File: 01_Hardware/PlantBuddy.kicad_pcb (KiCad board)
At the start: 2 copper layers, 35 x 87.3 mm, 36 parts, among them J101 J-Link SWD, J102 NFC Antenna, J2 Conn_I2C_SDA, J3 Conn_I2C_SCL, Q101 AO3401A, U101 nRF52832-QFxx, U102 LTR-303ALS-01, U6 SHTC3, Y1 32MHz, Y2 32kHz

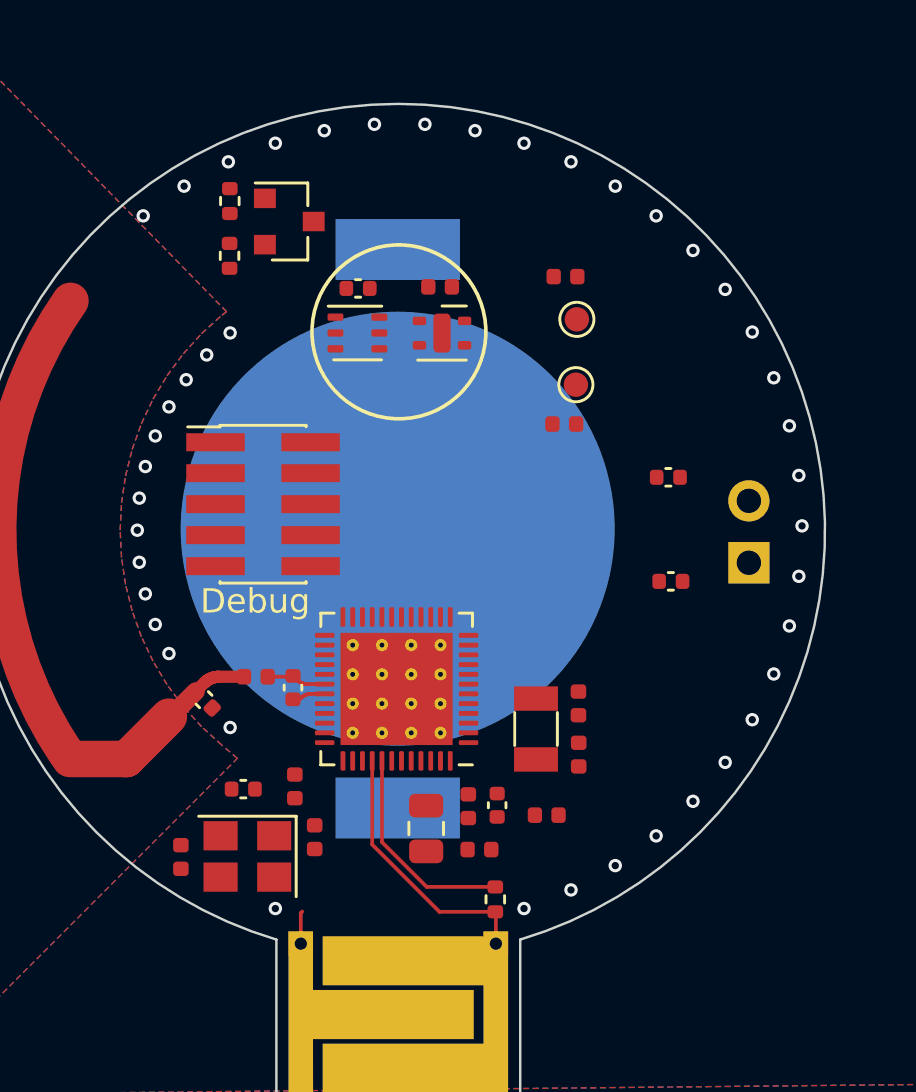
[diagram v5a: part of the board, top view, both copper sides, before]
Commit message: Switched to 0603 and re-did layout.
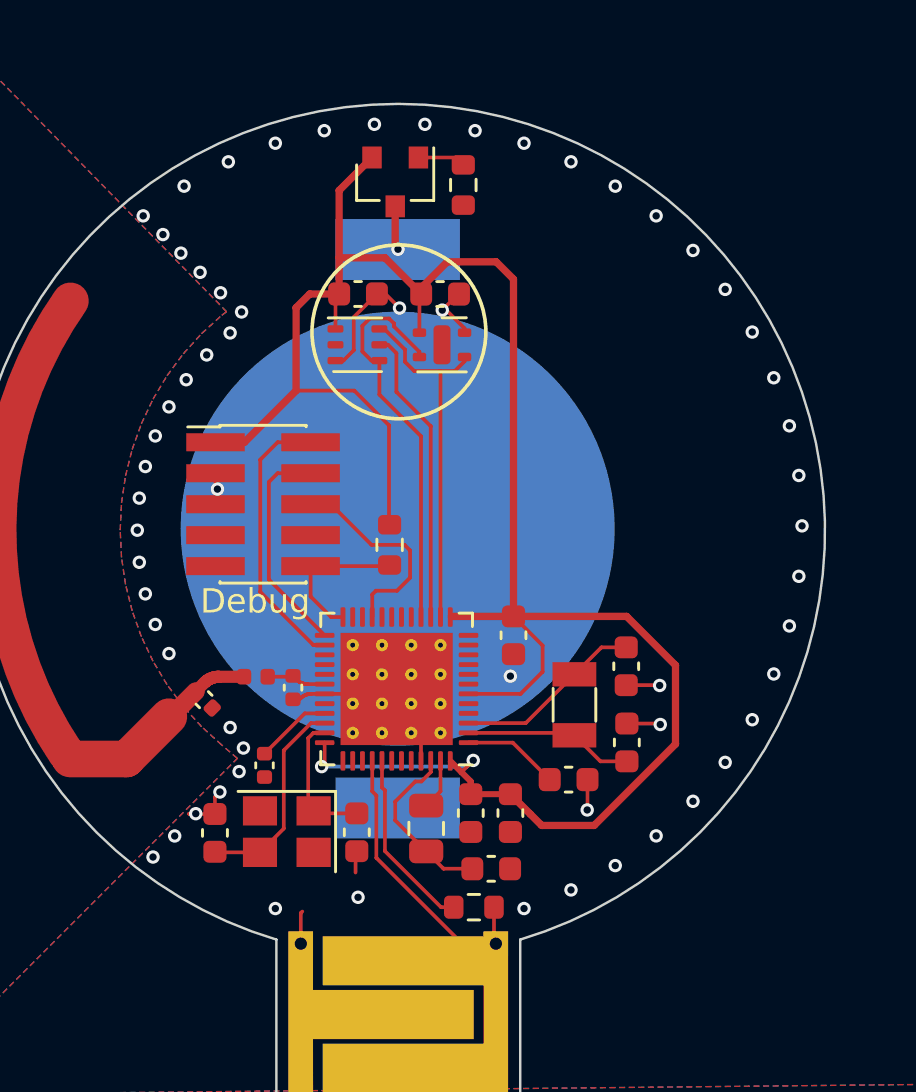
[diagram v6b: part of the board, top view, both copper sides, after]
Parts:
- removed C101, C102: N/P, Capacitor_SMD:C_0402_1005Metric
- removed J102: NFC Antenna, Connector_PinHeader_2.54mm:PinHeader_1x02_P2.54mm_Vertical
- removed J2: Conn_I2C_SDA, TestPoint:TestPoint_Pad_D1.0mm
- removed J3: Conn_I2C_SCL, TestPoint:TestPoint_Pad_D1.0mm
- removed R14, R15: 10k, Resistor_SMD:R_0402_1005Metric
- C10, C11, C12, C13, C14, C15, C16, C17, C3, C5, C6: footprint Capacitor_SMD:C_0402_1005Metric -> Capacitor_SMD:C_0603_1608Metric
- R1, R4: footprint Resistor_SMD:R_0402_1005Metric -> Resistor_SMD:R_0603_1608Metric
- R101: value 100k -> 3M3; footprint Resistor_SMD:R_0402_1005Metric -> Resistor_SMD:R_0603_1608Metric
- moved R1 13.5 mm to (65.4, 65.0)
- moved C10 10.9 mm to (70.4, 68.7)
- moved R4 9.60 mm to (68.4, 50.3)
- moved Q101 4.64 mm to (65.6, 50.1), turned to 270 degrees
- moved C13 2.48 mm to (75.1, 70.0)
- moved C14 2.04 mm to (75.1, 73.1)
- moved Y1 1.91 mm to (61.1, 76.8)
- moved Y2 1.86 mm to (72.9, 71.6)
- moved C6 1.74 mm to (64.0, 76.8)
- moved C5 1.71 mm to (72.7, 74.6)
- moved C11 1.71 mm to (58.2, 76.8)
- moved C9 1.31 mm to (60.2, 74.1), turned to 90 degrees
- moved R101 0.94 mm to (68.8, 79.9), turned to 0 degrees
- moved C16 0.92 mm to (69.5, 78.3)
- moved C15 0.63 mm to (70.3, 76.0)
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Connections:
- J101 pad 9: +BATT -> Net-(J101-Pad9)
- U101 pad 15: /SCL -> /LUX_INT
- U101 pad 16: Net-(U101-Pad16) -> /SCL
- U101 pad 18: /LUX_INT -> Net-(U101-Pad18)
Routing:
- net +BATT: track 0.00 -> 89.5 mm, vias 0 -> 2
- net GND: track 2.71 -> 24.5 mm, vias 43 -> 62
- net /SCL: track 0.00 -> 16.4 mm
- net /SDA: track 0.00 -> 14.9 mm
- net /LUX_INT: track 0.00 -> 12.2 mm
- net /SWDIO: track 0.00 -> 11.3 mm
- net /SWCLK: track 0.00 -> 9.10 mm
- net /SWO: track 0.00 -> 8.74 mm
- net /XC1: track 0.00 -> 8.58 mm
- net /XL2: track 0.00 -> 7.75 mm
- net Net-(C16-Pad2): track 0.00 -> 7.17 mm
- net /XL1: track 0.00 -> 6.98 mm
- net /~RST: track 0.00 -> 6.18 mm
- net /XC2: track 0.00 -> 5.60 mm
- net Net-(C5-Pad2): track 0.00 -> 3.96 mm
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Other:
- board text removed: "NFC"

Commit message: Done with latest HW revision. To be ordered with Aisler.
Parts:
- added LS101: Speaker_Crystal, Connector_PinHeader_2.54mm:PinHeader_1x02_P2.54mm_Vertical, F.Cu at (79.9, 65.4)
- moved C14 1.40 mm to (76.5, 73.1)
- moved Y2 1.40 mm to (74.3, 71.6)
- moved C13 1.40 mm to (76.5, 70.0)
- moved C5 1.40 mm to (74.1, 74.6)
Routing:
- net Net-(LS101-Pad2): track 0.00 -> 16.1 mm, vias 0 -> 2
- net Net-(LS101-Pad1): track 0.00 -> 15.7 mm, vias 0 -> 2
- net +BATT: track 89.5 -> 96.6 mm
- net /XL1: track 6.98 -> 8.37 mm
- net Net-(C5-Pad2): track 3.96 -> 5.35 mm
- net /XL2: track 7.75 -> 9.15 mm
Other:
- board text added: "FlivzNexxy"
- board text added: "Piezo"
- board text removed: "PlantBuddy"

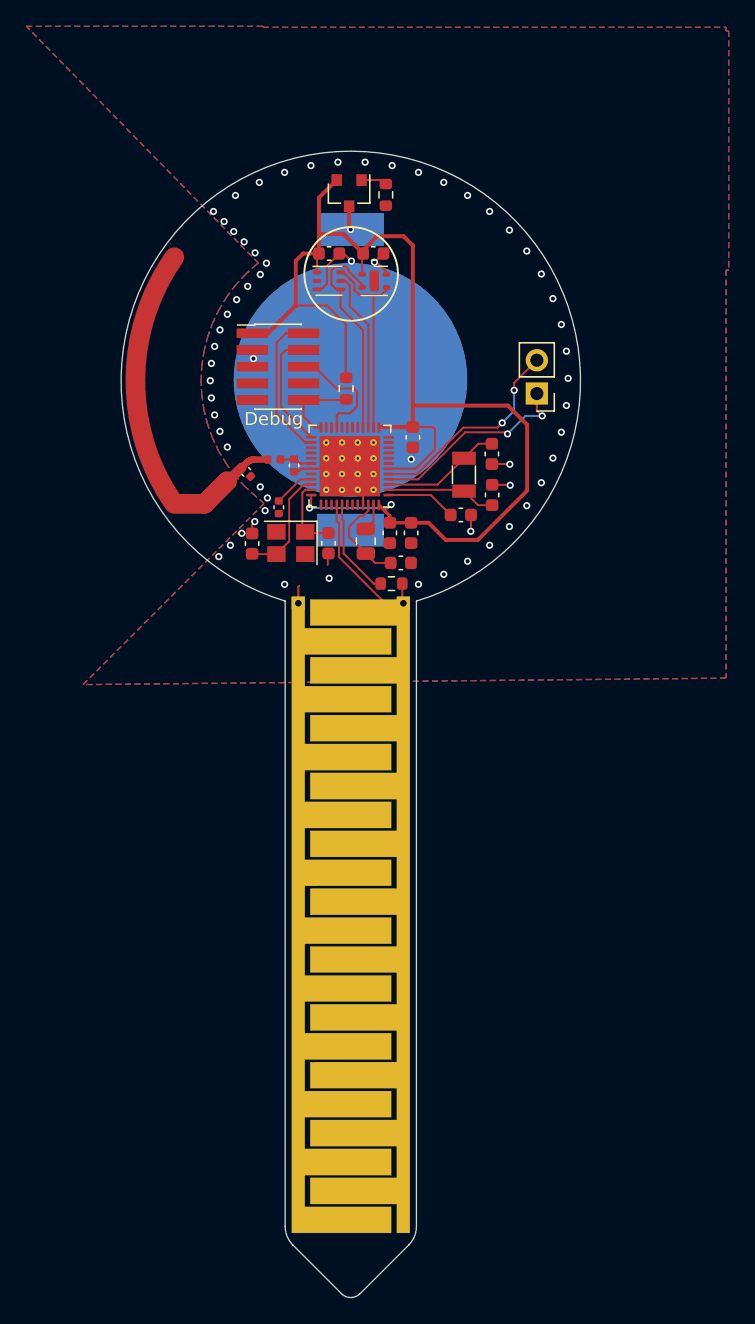
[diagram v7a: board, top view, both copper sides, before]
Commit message: Slight adjustments to Antenna ground plane & length.
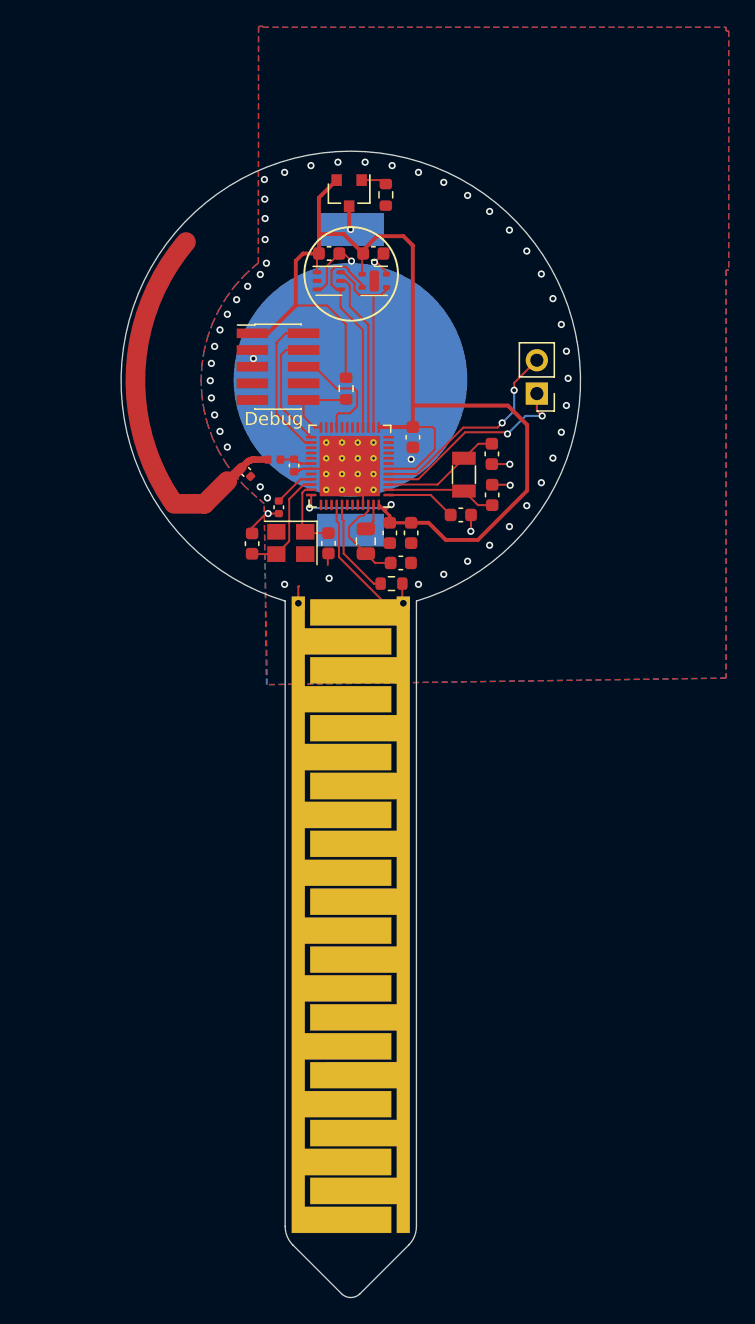
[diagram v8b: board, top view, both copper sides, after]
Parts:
- turned AE101 to 139.9 degrees
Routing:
- net GND: track 24.5 -> 25.4 mm, vias 62 -> 55
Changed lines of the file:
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@@
     (thickness 1.6)
     (drawings 21)
-    (tracks 328)
+    (tracks 321)
     (zones 0)
     (modules 30)
@@
     (uvia_drill 0.1)
   )
+  (module PlantBuddy:monopole (layer F.Cu)
+    (at 65.7098 64.4144 139.9)
+    (fp_text reference AE101 (at 0 0 319.9) (layer F.SilkS) hide
+      (effects (font (size 1.27 1.27) (thickness 0.15)))
+    )
+    (fp_text value Antenna (at 0 0 319.9) (layer F.SilkS) hide
+      (effects (font (size 1.27 1.27) (thickness 0.15)))
+    )
+    (fp_arc (start 0 0) (end 16.4 0) (angle -74) (layer F.Cu) (width 1.5))
+  )
   (module Connector_PinHeader_2.54mm:PinHeader_1x02_P2.54mm_Vertical (layer F.Cu)
     (at 79.89228 65.396371 180)
@@
     )
     (fp_text value Speaker_Crystal (at 0 4.87) (layer F.Fab)
-      (effects (font (size 1 1) (thickness 0.15)))
-    )
-    (fp_text user %R (at 0 1.27 90) (layer F.Fab)
       (effects (font (size 1 1) (thickness 0.15)))
     )
@@
     (fp_line (start 1.8 4.35) (end 1.8 -1.8) (layer F.CrtYd) (width 0.05))
     (fp_line (start 1.8 -1.8) (end -1.8 -1.8) (layer F.CrtYd) (width 0.05))
+    (fp_text user %R (at 0 1.27 90) (layer F.Fab)
+      (effects (font (size 1 1) (thickness 0.15)))
+    )
     (pad 2 thru_hole oval (at 0 2.54 180) (size 1.7 1.7) (drill 1) (layers *.Cu *.Mask)
       (net 53 "Net-(LS101-Pad2)"))
@@
       (rotate (xyz 0 0 0))
     )
-  )
-  (module PlantBuddy:monopole (layer F.Cu)
-    (at 65.7098 64.4144 145)
-    (fp_text reference AE101 (at 0 0 325) (layer F.SilkS) hide
-      (effects (font (size 1.27 1.27) (thickness 0.15)))
-    )
-    (fp_text value Antenna (at 0 0 325) (layer F.SilkS) hide
-      (effects (font (size 1.27 1.27) (thickness 0.15)))
-    )
-    (fp_arc (start 0 0) (end 16.4 0) (angle -68.9) (layer F.Cu) (width 1.5))
   )
   (module Capacitor_SMD:C_0402_1005Metric (layer F.Cu)
@@
   (via (at 62.684208 48.02886) (size 0.55) (drill 0.3) (layers F.Cu B.Cu) (net 6))
   (via (at 60.67722 48.544167) (size 0.55) (drill 0.3) (layers F.Cu B.Cu) (net 6))
-  (via (at 58.750642 49.306954) (size 0.55) (drill 0.3) (layers F.Cu B.Cu) (net 6))
-  (via (at 56.934858 50.305189) (size 0.55) (drill 0.3) (layers F.Cu B.Cu) (net 6))
-  (via (at 55.258504 51.523131) (size 0.55) (drill 0.3) (layers F.Cu B.Cu) (net 6))
+  (via (at 59.14048 49.089571) (size 0.55) (drill 0.3) (layers F.Cu B.Cu) (net 6))
   (segment (start 61.72212 81.36878) (end 61.72212 80.112131) (width 0.1524) (layer F.Cu) (net 6))
   (segment (start 61.72212 80.112131) (end 61.78208 80.052171) (width 0.1524) (layer F.Cu) (net 6))
@@
   (via (at 64.06808 79.467971) (size 0.55) (drill 0.3) (layers F.Cu B.Cu) (net 6))
   (segment (start 63.96648 77.575971) (end 63.96648 78.451971) (width 0.1524) (layer F.Cu) (net 6))
-  (via (at 57.41328 76.038971) (size 0.55) (drill 0.3) (layers F.Cu B.Cu) (net 6))
-  (segment (start 57.14628 76.051371) (end 57.13388 76.038971) (width 0.1524) (layer F.Cu) (net 6))
-  (segment (start 58.20068 76.051371) (end 57.14628 76.051371) (width 0.1524) (layer F.Cu) (net 6))
-  (via (at 59.19128 74.311771) (size 0.55) (drill 0.3) (layers F.Cu B.Cu) (net 6))
-  (via (at 58.40388 75.149971) (size 0.55) (drill 0.3) (layers F.Cu B.Cu) (net 6))
-  (via (at 56.54968 76.953371) (size 0.55) (drill 0.3) (layers F.Cu B.Cu) (net 6))
-  (via (at 55.66068 77.816971) (size 0.55) (drill 0.3) (layers F.Cu B.Cu) (net 6))
-  (via (at 56.06708 52.289971) (size 0.55) (drill 0.3) (layers F.Cu B.Cu) (net 6))
-  (via (at 56.80368 53.051971) (size 0.55) (drill 0.3) (layers F.Cu B.Cu) (net 6))
-  (via (at 57.59108 53.839371) (size 0.55) (drill 0.3) (layers F.Cu B.Cu) (net 6))
-  (via (at 58.42928 54.677571) (size 0.55) (drill 0.3) (layers F.Cu B.Cu) (net 6))
   (via (at 59.29288 55.464971) (size 0.55) (drill 0.3) (layers F.Cu B.Cu) (net 6))
-  (segment (start 58.20068 75.353171) (end 58.40388 75.149971) (width 0.1524) (layer F.Cu) (net 6))
-  (segment (start 58.20068 76.051371) (end 58.20068 75.353171) (width 0.1524) (layer F.Cu) (net 6))
   (via (at 58.30228 62.729371) (size 0.55) (drill 0.3) (layers F.Cu B.Cu) (net 6))
   (segment (start 58.2734 62.700491) (end 58.30228 62.729371) (width 0.1524) (layer F.Cu) (net 6))
@@
   (via (at 60.67722 79.929033) (size 0.55) (drill 0.3) (layers F.Cu B.Cu) (net 6))
   (via (at 59.36908 73.346571) (size 0.55) (drill 0.3) (layers F.Cu B.Cu) (net 6))
+  (via (at 59.16588 50.588171) (size 0.55) (drill 0.3) (layers F.Cu B.Cu) (net 6))
+  (via (at 59.19128 52.061371) (size 0.55) (drill 0.3) (layers F.Cu B.Cu) (net 6))
+  (via (at 59.19128 53.661571) (size 0.55) (drill 0.3) (layers F.Cu B.Cu) (net 6))
+  (segment (start 59.27008 74.537771) (end 59.42248 74.537771) (width 0.1524) (layer F.Cu) (net 6))
+  (segment (start 58.20068 75.607171) (end 59.27008 74.537771) (width 0.1524) (layer F.Cu) (net 6))
+  (segment (start 58.20068 76.051371) (end 58.20068 75.607171) (width 0.1524) (layer F.Cu) (net 6))
+  (segment (start 59.42248 74.537771) (end 60.23268 74.537771) (width 0.1524) (layer F.Cu) (net 6))
+  (via (at 59.42248 74.537771) (size 0.55) (drill 0.3) (layers F.Cu B.Cu) (net 6))
   (segment (start 64.9432 56.8092) (end 65.297266 56.8092) (width 0.1524) (layer F.Cu) (net 7))
   (segment (start 65.297266 56.8092) (end 65.64288 57.154814) (width 0.1524) (layer F.Cu) (net 7))
@@
   (segment (start 67.47168 79.874371) (end 65.171701 77.574392) (width 0.1524) (layer F.Cu) (net 21))
   (segment (start 67.99288 79.874371) (end 67.47168 79.874371) (width 0.1524) (layer F.Cu) (net 21))
-  (segment (start 68.6001 71.9256) (end 70.854619 71.9256) (width 0.1524) (layer F.Cu) (net 54))
-  (segment (start 70.854619 71.9256) (end 74.437448 68.342771) (width 0.1524) (layer F.Cu) (net 54))
   (via (at 65.706377 52.891763) (size 0.55) (drill 0.3) (layers F.Cu B.Cu) (net 39))
   (segment (start 65.59208 52.777466) (end 65.706377 52.891763) (width 0.3) (layer F.Cu) (net 39))
@@
   (segment (start 78.16508 66.717171) (end 78.16508 65.142371) (width 0.1524) (layer B.Cu) (net 53))
   (segment (start 78.16508 64.583571) (end 78.16508 65.142371) (width 0.1524) (layer F.Cu) (net 53))
+  (segment (start 68.6001 71.9256) (end 70.854619 71.9256) (width 0.1524) (layer F.Cu) (net 54))
+  (segment (start 70.854619 71.9256) (end 74.437448 68.342771) (width 0.1524) (layer F.Cu) (net 54))
   (via (at 77.65708 68.469771) (size 0.55) (drill 0.3) (layers F.Cu B.Cu) (net 54))
   (segment (start 77.53008 68.342771) (end 77.65708 68.469771) (width 0.1524) (layer F.Cu) (net 54))
@@
       (pts
         (xy 94.3102 37.7698) (xy 94.5134 37.7698) (xy 94.5134 55.9816) (xy 94.3102 55.9816) (xy 94.3102 87.0712)
-        (xy 45.324452 87.568349) (xy 59.120349 73.772452) (xy 58.482234 73.224528) (xy 57.6533 72.473226) (xy 56.901998 71.644292)
+        (xy 59.36908 87.568349) (xy 59.120349 73.772452) (xy 58.482234 73.224528) (xy 57.6533 72.473226) (xy 56.901998 71.644292)
         (xy 56.235564 70.745709) (xy 55.660415 69.786131) (xy 55.182091 68.7748) (xy 54.805198 67.721454) (xy 54.533365 66.636238)
         (xy 54.369212 65.529604) (xy 54.314317 64.412209) (xy 54.369212 63.294814) (xy 54.533365 62.18818) (xy 54.805198 61.102964)
         (xy 55.182091 60.049618) (xy 55.660415 59.038287) (xy 56.235564 58.078709) (xy 56.901998 57.180126) (xy 57.6533 56.351192)
-        (xy 58.482234 55.59989) (xy 58.679436 55.453636) (xy 40.9956 37.4142) (xy 59.0296 37.4142) (xy 59.0296 37.4904)
+        (xy 58.482234 55.59989) (xy 58.679436 55.453636) (xy 58.70868 37.4142) (xy 59.0296 37.4142) (xy 59.0296 37.4904)
         (xy 94.3102 37.4904)
       )
@@
       (pts
         (xy 94.3102 37.7698) (xy 94.5134 37.7698) (xy 94.5134 55.9816) (xy 94.3102 55.9816) (xy 94.3102 87.0712)
-        (xy 45.324452 87.568349) (xy 59.120349 73.772452) (xy 58.482234 73.224528) (xy 57.6533 72.473226) (xy 56.901998 71.644292)
+        (xy 59.29288 87.568349) (xy 59.120349 73.772452) (xy 58.482234 73.224528) (xy 57.6533 72.473226) (xy 56.901998 71.644292)
         (xy 56.235564 70.745709) (xy 55.660415 69.786131) (xy 55.182091 68.7748) (xy 54.805198 67.721454) (xy 54.533365 66.636238)
         (xy 54.369212 65.529604) (xy 54.314317 64.412209) (xy 54.369212 63.294814) (xy 54.533365 62.18818) (xy 54.805198 61.102964)
         (xy 55.182091 60.049618) (xy 55.660415 59.038287) (xy 56.235564 58.078709) (xy 56.901998 57.180126) (xy 57.6533 56.351192)
-        (xy 58.482234 55.59989) (xy 58.679436 55.453636) (xy 40.9956 37.4142) (xy 59.0296 37.4142) (xy 59.0296 37.4904)
+        (xy 58.482234 55.59989) (xy 58.679436 55.453636) (xy 58.68328 37.456371) (xy 59.0296 37.4142) (xy 59.0296 37.4904)
         (xy 94.3102 37.4904)
       )
